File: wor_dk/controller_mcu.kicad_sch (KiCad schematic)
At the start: 54 parts, among them J201 USB_A, J202 Prog, J203 u.FL, SW201 SW_Push, SW202 SW_Push, U201 nRF52840, Y201 32MHz, Y202 32.768kHz

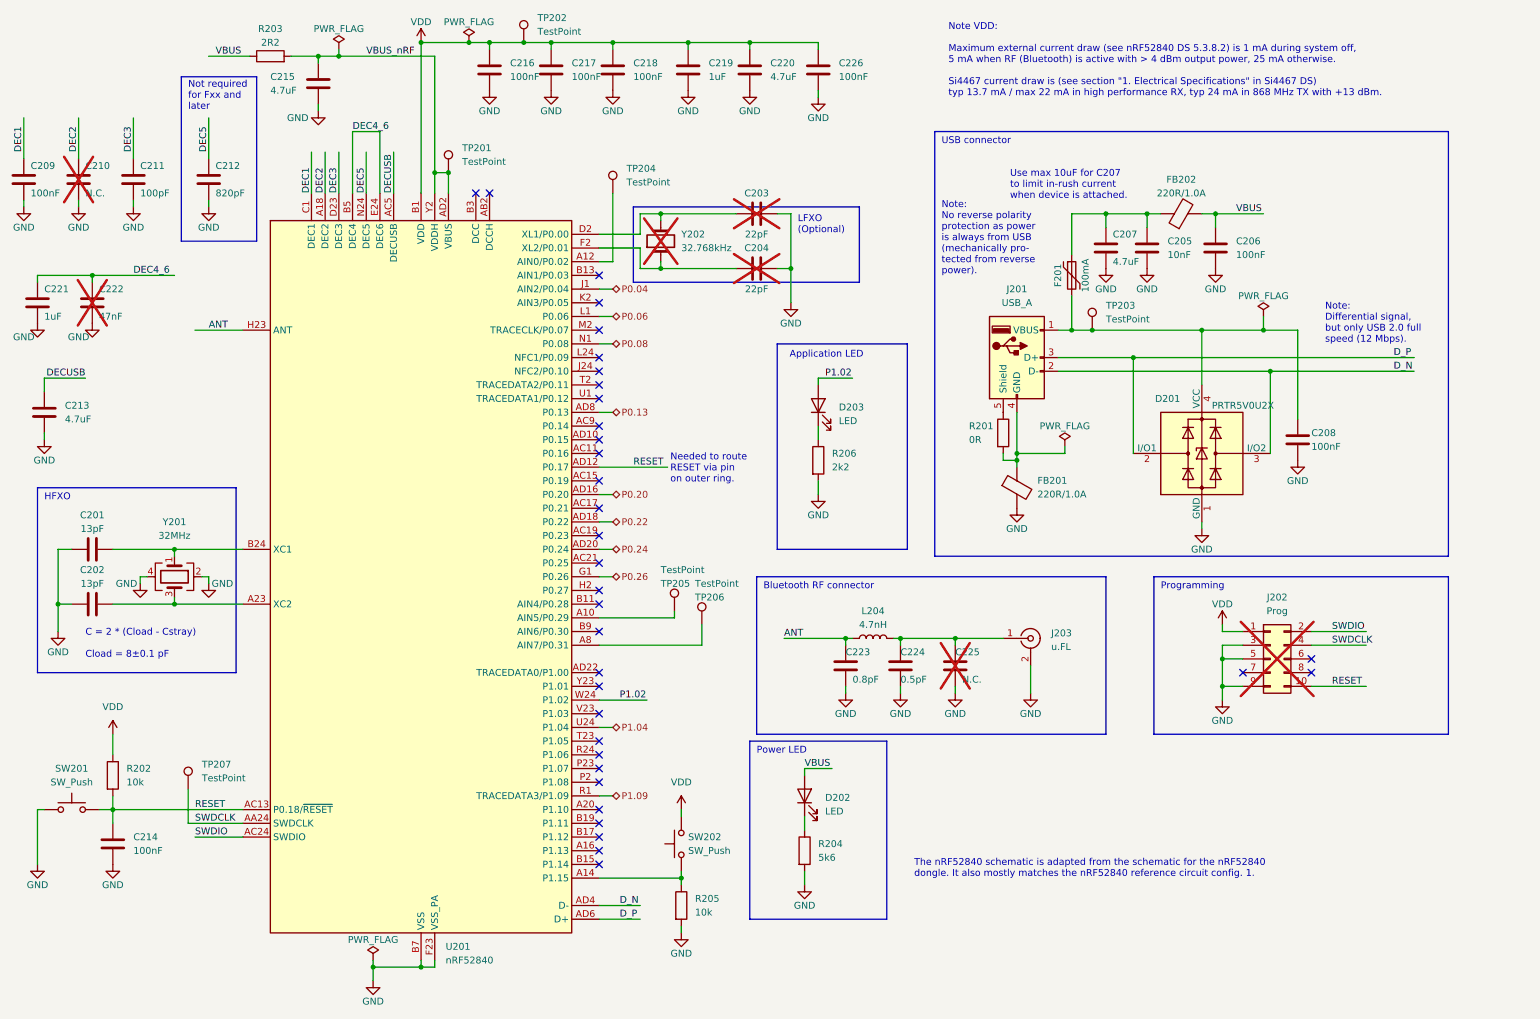
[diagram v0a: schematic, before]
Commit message: wor_dk: add top-level hierarchical sheets & update annotation
- import hierarchical sheet for main MCU
- import hierarchical sheet for transceiver MCU
- import hierarchical sheet for controller MCU
- update annotations for controller MCU
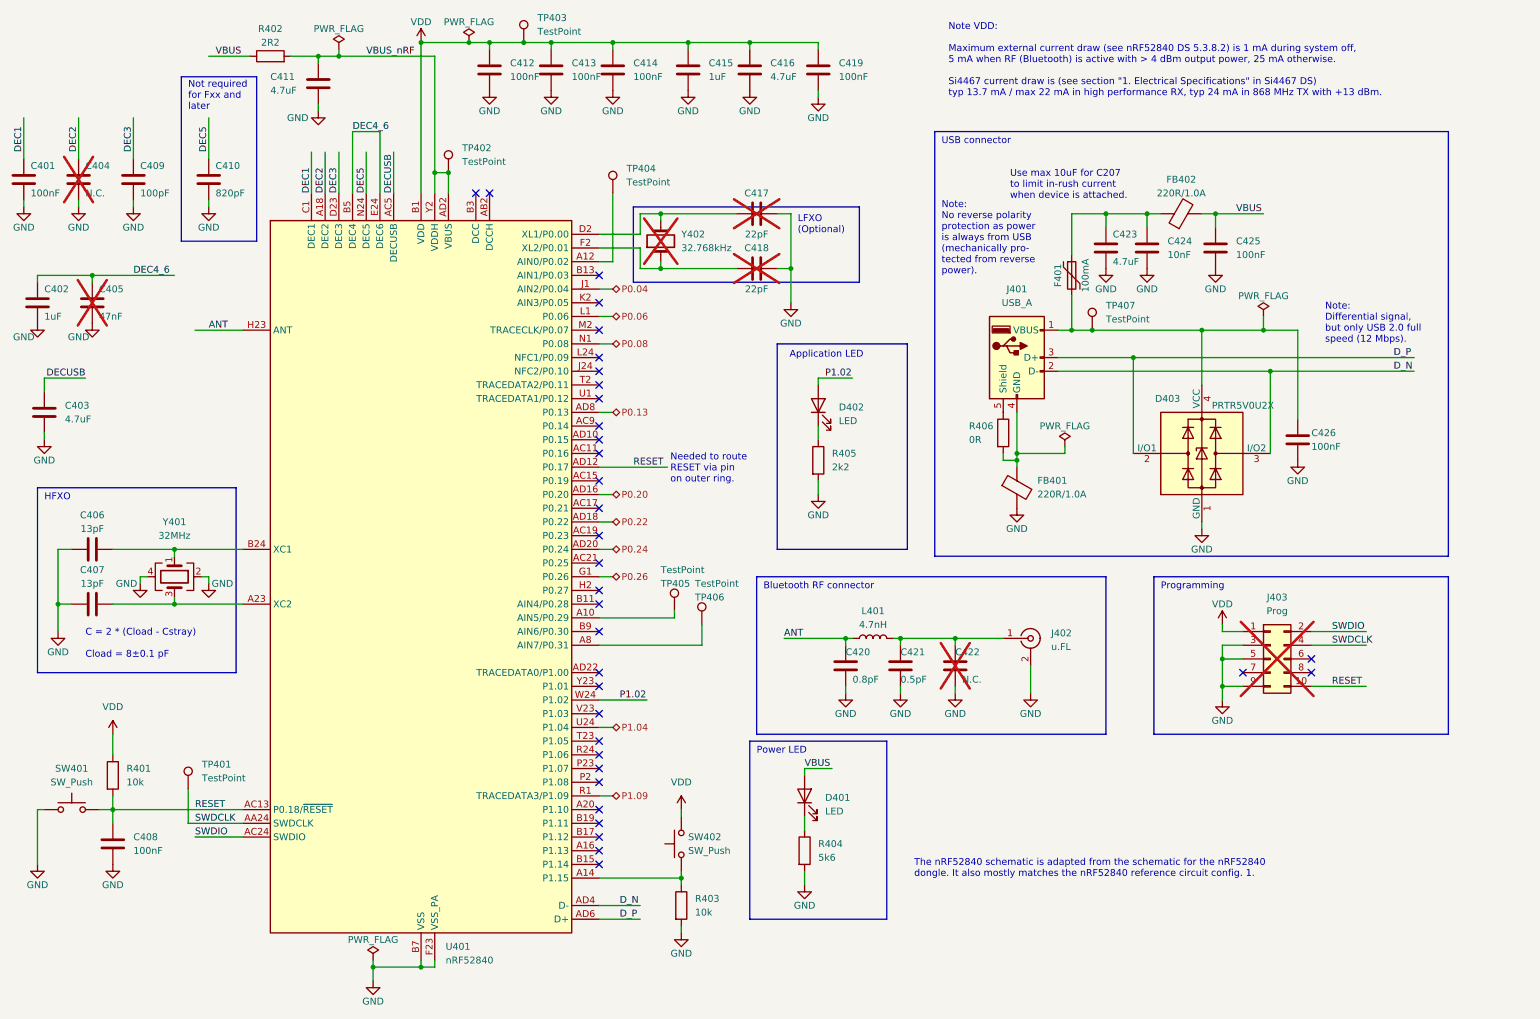
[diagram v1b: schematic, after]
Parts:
- removed C201, C202: 13pF, Capacitor_SMD:C_0402_1005Metric, symbol Device:C
- removed C203, C204: 22pF, Capacitor_SMD:C_0402_1005Metric, symbol Device:C
- removed C205: 10nF, Capacitor_SMD:C_0201_0603Metric, symbol Device:C
- removed C206, C208, C209, C214, C216, C217, C218, C226: 100nF, Capacitor_SMD:C_0201_0603Metric, symbol Device:C
- removed C207, C215: 4.7uF, Capacitor_SMD:C_0402_1005Metric, symbol Device:C
- removed C210, C225: N.C., Capacitor_SMD:C_0201_0603Metric, symbol Device:C
- removed C211: 100pF, Capacitor_SMD:C_0201_0603Metric, symbol Device:C
- removed C212: 820pF, Capacitor_SMD:C_0201_0603Metric, symbol Device:C
- removed C213, C220: 4.7uF, Capacitor_SMD:C_0603_1608Metric, symbol Device:C
- removed C219, C221: 1uF, Capacitor_SMD:C_0603_1608Metric, symbol Device:C
- removed C222: 47nF, Capacitor_SMD:C_0201_0603Metric, symbol Device:C
- removed C223: 0.8pF, Capacitor_SMD:C_0201_0603Metric, symbol Device:C
- removed C224: 0.5pF, Capacitor_SMD:C_0201_0603Metric, symbol Device:C
- removed D201: PRTR5V0U2X, Package_TO_SOT_SMD:SOT-143, symbol Power_Protection:PRTR5V0U2X
- removed D202, D203: LED, LED_SMD:LED_0805_2012Metric, symbol Device:LED
- removed F201: 100mA, Fuse:Fuse_0603_1608Metric, symbol Device:Polyfuse
- removed FB201, FB202: 220R/1.0A, Resistor_SMD:R_0402_1005Metric, symbol Device:FerriteBead
- removed J201: USB_A, Connector_USB:USB_A_CNCTech_1001-011-01101_Horizontal, symbol Connector:USB_A
- removed J202: Prog, Connector_PinHeader_1.27mm:PinHeader_2x05_P1.27mm_Vertical_SMD, symbol Connector_Generic:Conn_02x05_Odd_Even
- removed J203: u.FL, Connector_Coaxial:U.FL_Hirose_U.FL-R-SMT-1_Vertical, symbol Connector:Conn_Coaxial
- removed L204: 4.7nH, Inductor_SMD:L_0201_0603Metric, symbol Device:L
- removed R201: 0R, Resistor_SMD:R_0402_1005Metric, symbol Device:R
- removed R202, R205: 10k, Resistor_SMD:R_0402_1005Metric, symbol Device:R
- removed R203: 2R2, Resistor_SMD:R_0201_0603Metric, symbol Device:R
- removed R204: 5k6, Resistor_SMD:R_0402_1005Metric, symbol Device:R
- removed R206: 2k2, Resistor_SMD:R_0402_1005Metric, symbol Device:R
- removed SW201, SW202: SW_Push, Button_Switch_SMD:SW_SPST_PTS810, symbol Switch:SW_Push
- removed TP201, TP202, TP203, TP204, TP205, TP206, TP207: TestPoint, TestPoint:TestPoint_Pad_D1.0mm, symbol Connector:TestPoint
- removed U201: nRF52840, Package_DFN_QFN:Nordic_AQFN-73-1EP_7x7mm_P0.5mm, symbol MCU_Nordic:nRF52840
- removed Y201: 32MHz, Crystal:Crystal_SMD_2016-4Pin_2.0x1.6mm, symbol Device:Crystal_GND24
- removed Y202: 32.768kHz, Crystal:Crystal_SMD_3215-2Pin_3.2x1.5mm, symbol Device:Crystal
- added C401, C408, C412, C413, C414, C419, C425, C426: 100nF, Capacitor_SMD:C_0201_0603Metric, symbol Device:C
- added C402, C415: 1uF, Capacitor_SMD:C_0603_1608Metric, symbol Device:C
- added C403, C416: 4.7uF, Capacitor_SMD:C_0603_1608Metric, symbol Device:C
- added C404, C422: N.C., Capacitor_SMD:C_0201_0603Metric, symbol Device:C
- added C405: 47nF, Capacitor_SMD:C_0201_0603Metric, symbol Device:C
- added C406, C407: 13pF, Capacitor_SMD:C_0402_1005Metric, symbol Device:C
- added C409: 100pF, Capacitor_SMD:C_0201_0603Metric, symbol Device:C
- added C410: 820pF, Capacitor_SMD:C_0201_0603Metric, symbol Device:C
- added C411, C423: 4.7uF, Capacitor_SMD:C_0402_1005Metric, symbol Device:C
- added C417, C418: 22pF, Capacitor_SMD:C_0402_1005Metric, symbol Device:C
- added C420: 0.8pF, Capacitor_SMD:C_0201_0603Metric, symbol Device:C
- added C421: 0.5pF, Capacitor_SMD:C_0201_0603Metric, symbol Device:C
- added C424: 10nF, Capacitor_SMD:C_0201_0603Metric, symbol Device:C
- added D401, D402: LED, LED_SMD:LED_0805_2012Metric, symbol Device:LED
- added D403: PRTR5V0U2X, Package_TO_SOT_SMD:SOT-143, symbol Power_Protection:PRTR5V0U2X
- added F401: 100mA, Fuse:Fuse_0603_1608Metric, symbol Device:Polyfuse
- added FB401, FB402: 220R/1.0A, Resistor_SMD:R_0402_1005Metric, symbol Device:FerriteBead
- added J401: USB_A, Connector_USB:USB_A_CNCTech_1001-011-01101_Horizontal, symbol Connector:USB_A
- added J402: u.FL, Connector_Coaxial:U.FL_Hirose_U.FL-R-SMT-1_Vertical, symbol Connector:Conn_Coaxial
- added J403: Prog, Connector_PinHeader_1.27mm:PinHeader_2x05_P1.27mm_Vertical_SMD, symbol Connector_Generic:Conn_02x05_Odd_Even
- added L401: 4.7nH, Inductor_SMD:L_0201_0603Metric, symbol Device:L
- added R401, R403: 10k, Resistor_SMD:R_0402_1005Metric, symbol Device:R
- added R402: 2R2, Resistor_SMD:R_0201_0603Metric, symbol Device:R
- added R404: 5k6, Resistor_SMD:R_0402_1005Metric, symbol Device:R
- added R405: 2k2, Resistor_SMD:R_0402_1005Metric, symbol Device:R
- added R406: 0R, Resistor_SMD:R_0402_1005Metric, symbol Device:R
- added SW401, SW402: SW_Push, Button_Switch_SMD:SW_SPST_PTS810, symbol Switch:SW_Push
- added TP401, TP402, TP403, TP404, TP405, TP406, TP407: TestPoint, TestPoint:TestPoint_Pad_D1.0mm, symbol Connector:TestPoint
- added U401: nRF52840, Package_DFN_QFN:Nordic_AQFN-73-1EP_7x7mm_P0.5mm, symbol MCU_Nordic:nRF52840
- added Y401: 32MHz, Crystal:Crystal_SMD_2016-4Pin_2.0x1.6mm, symbol Device:Crystal_GND24
- added Y402: 32.768kHz, Crystal:Crystal_SMD_3215-2Pin_3.2x1.5mm, symbol Device:Crystal
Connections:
- net ANT: now also C420.1, L401.1, U401.H23 (ANT)
- net DEC1: now also C401.1, U401.C1 (DEC1)
- net DEC2: now also C404.1, U401.A18 (DEC2)
- net DEC3: now also C409.1, U401.D23 (DEC3)
- net DEC4_6: now also C402.1, C405.1, U401.B5 (DEC4), U401.E24 (DEC6)
- net DEC5: now also C410.1, U401.N24 (DEC5)
- net DECUSB: now also C403.2, U401.AC5 (DECUSB)
- net D_N: now also D403.3 (I/O2), J401.2 (D-), U401.AD4 (D-)
- net D_P: now also D403.2 (I/O1), J401.3 (D+), U401.AD6 (D+)
- net GND: now also C401.2, C402.2, C403.1, C404.2, C405.2, C406.1, C407.1, C408.2, C409.2, C410.2, C411.2, C412.2, C413.2, C414.2, C415.2, C416.2, C417.1, C418.2, C419.2, C420.2, C421.2, C422.2, C423.2, C424.2, C425.2, C426.2, D403.1 (GND), FB401.2, J402.2 (Ext), J403.3 (Pin_3), J403.5 (Pin_5), J403.9 (Pin_9), R403.2, R404.2, R405.2, SW401.1, U401.B7 (VSS), U401.EP (VSS), U401.F23 (VSS_PA), Y401.2, Y401.4
- net P0.04: now also U401.J1 (AIN2/P0.04)
- net P0.06: now also U401.L1 (P0.06)
- net P0.08: now also U401.N1 (P0.08)
- net P0.13: now also U401.AD8 (P0.13)
- net P0.20: now also U401.AD16 (P0.20)
- net P0.22: now also U401.AD18 (P0.22)
- net P0.24: now also U401.AD20 (P0.24)
- net P0.26: now also U401.G1 (P0.26)
- net P1.02: now also D402.2 (A), U401.W24 (P1.02)
- net P1.04: now also U401.U24 (P1.04)
- net P1.09: now also U401.R1 (TRACEDATA3/P1.09)
- net RESET: now also C408.1, J403.10 (Pin_10), R401.2, SW401.2, U401.AC13 (P0.18/~{RESET}), U401.AD12 (P0.17)
- net SWDCLK: now also J403.4 (Pin_4), TP401.1, U401.AA24 (SWDCLK)
- net SWDIO: now also J403.2 (Pin_2), U401.AC24 (SWDIO)
- net VBUS: now also C425.1, D401.2 (A), FB402.2, R402.1
- net VBUS_nRF: now also C411.1, R402.2, TP402.1, U401.AD2 (VBUS), U401.Y2 (VDDH)
- net VDD: now also C412.1, C413.1, C414.1, C415.1, C416.1, C419.1, J403.1 (Pin_1), R401.1, SW402.2, TP403.1, U401.A22 (VDD), U401.AD14 (VDD), U401.AD23 (VDD), U401.B1 (VDD), U401.W1 (VDD)
- new net: C417.2, U401.D2 (XL1/P0.00), Y402.2
- new net: FB401.1, J401.4 (GND), R406.2
- new net: TP406.1, U401.A8 (AIN7/P0.31)
- new net: TP404.1, U401.A12 (AIN0/P0.02)
- new net: J401.5 (Shield), R406.1
- new net: C421.1, C422.1, J402.1 (In), L401.2
- new net: C423.1, C424.1, F401.1, FB402.1
- new net: C426.1, D403.4 (VCC), F401.2, J401.1 (VBUS), TP407.1
- new net: C406.2, U401.B24 (XC1), Y401.1
- new net: C418.1, U401.F2 (XL2/P0.01), Y402.1
- new net: TP405.1, U401.A10 (AIN5/P0.29)
- new net: R403.1, SW402.1, U401.A14 (P1.15)
- new net: C407.2, U401.A23 (XC2), Y401.3
- new net: D401.1 (K), R404.1
- new net: D402.1 (K), R405.1
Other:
- title: MCU -> Controller MCU

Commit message: wor_dk: high-level adjustments for main MCU, transceiver & controller
Main MCU:
- populate 32 kHz crystal (remove DNP)
- populate programming connector (remove DNP)
- remove power LED
- remove application LED
- remove user button
- remove Bluetooth parts
- remove USB connector & parts

Transceiver:
- remove RX/TX LEDs

Controller MCU:
- populate programming connector (remove DNP)
- remove 32 kHz crystal & capacitors
- remove Bluetooth parts
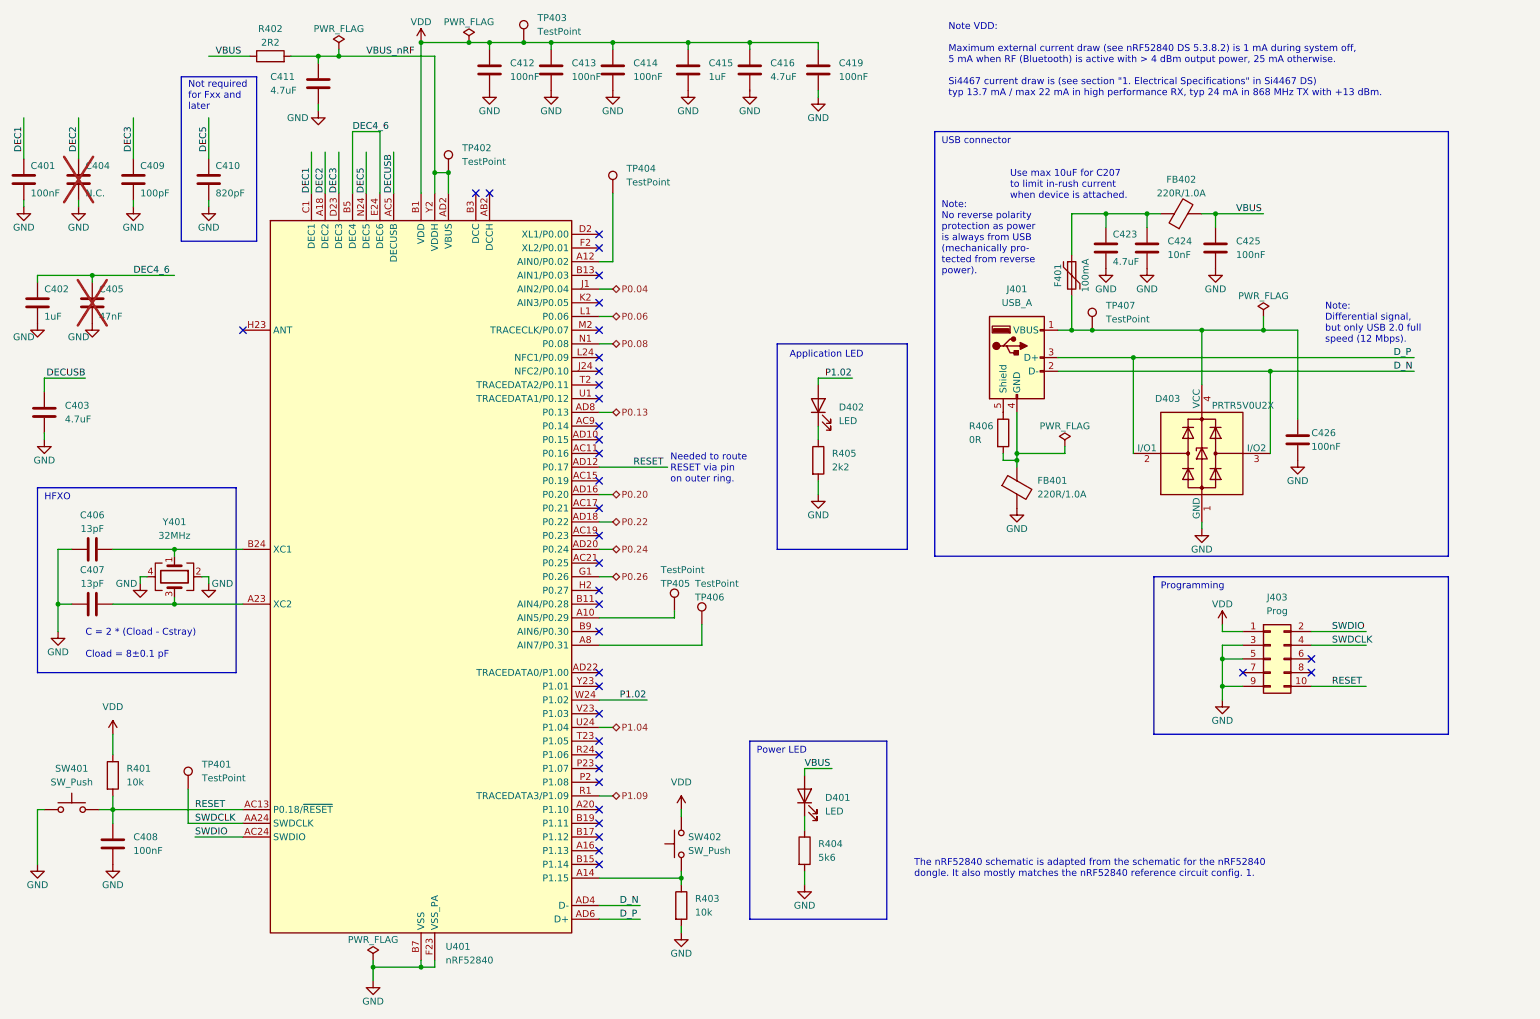
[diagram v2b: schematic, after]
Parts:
- removed C417, C418: 22pF, Capacitor_SMD:C_0402_1005Metric, symbol Device:C
- removed C420: 0.8pF, Capacitor_SMD:C_0201_0603Metric, symbol Device:C
- removed C421: 0.5pF, Capacitor_SMD:C_0201_0603Metric, symbol Device:C
- removed C422: N.C., Capacitor_SMD:C_0201_0603Metric, symbol Device:C
- removed J402: u.FL, Connector_Coaxial:U.FL_Hirose_U.FL-R-SMT-1_Vertical, symbol Connector:Conn_Coaxial
- removed L401: 4.7nH, Inductor_SMD:L_0201_0603Metric, symbol Device:L
- removed Y402: 32.768kHz, Crystal:Crystal_SMD_3215-2Pin_3.2x1.5mm, symbol Device:Crystal
- J403: now fitted
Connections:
- net ANT: no longer names the net of U401.H23 (ANT)
- no-connect marks 34 -> 37
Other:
- note removed: "Bluetooth RF connector"
- note removed: "LFXO (Optional)"

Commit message: wor_dk: adapt main MCU power supply to externally powered
The main MCU now has support for enabling DC/DC converter for REG1 as
per reference circuit configuration no. 5.
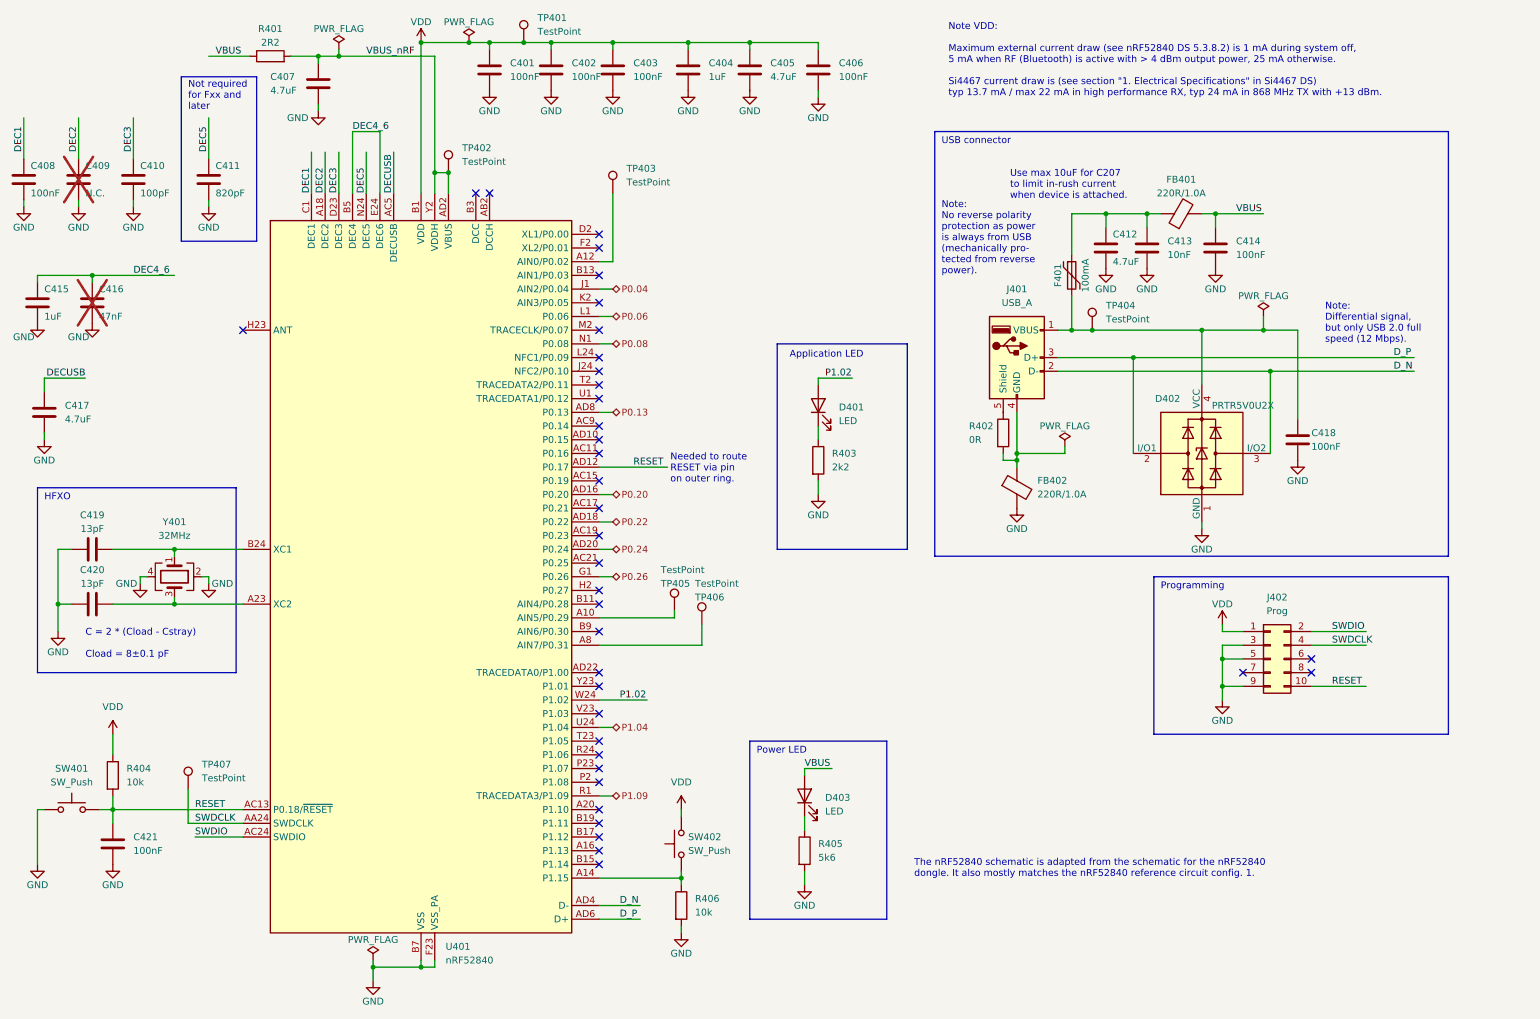
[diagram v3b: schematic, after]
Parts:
- renumbered C412 to C401, C413 to C402, C414 to C403, C415 to C404, C416 to C405, C419 to C406, C411 to C407, C401 to C408, C404 to C409, C409 to C410, C410 to C411, C423 to C412, C424 to C413, C425 to C414, C402 to C415, C405 to C416, C403 to C417, C426 to C418, C406 to C419, C407 to C420, C408 to C421, D402 to D401, D403 to D402, D401 to D403, FB402 to FB401, FB401 to FB402, J403 to J402, R402 to R401, R406 to R402, R405 to R403, R401 to R404, R404 to R405, R403 to R406, TP403 to TP401, TP404 to TP403, TP407 to TP404, TP401 to TP407
